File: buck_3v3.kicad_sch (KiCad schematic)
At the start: 20 parts, among them U6 TPS564257DRLR

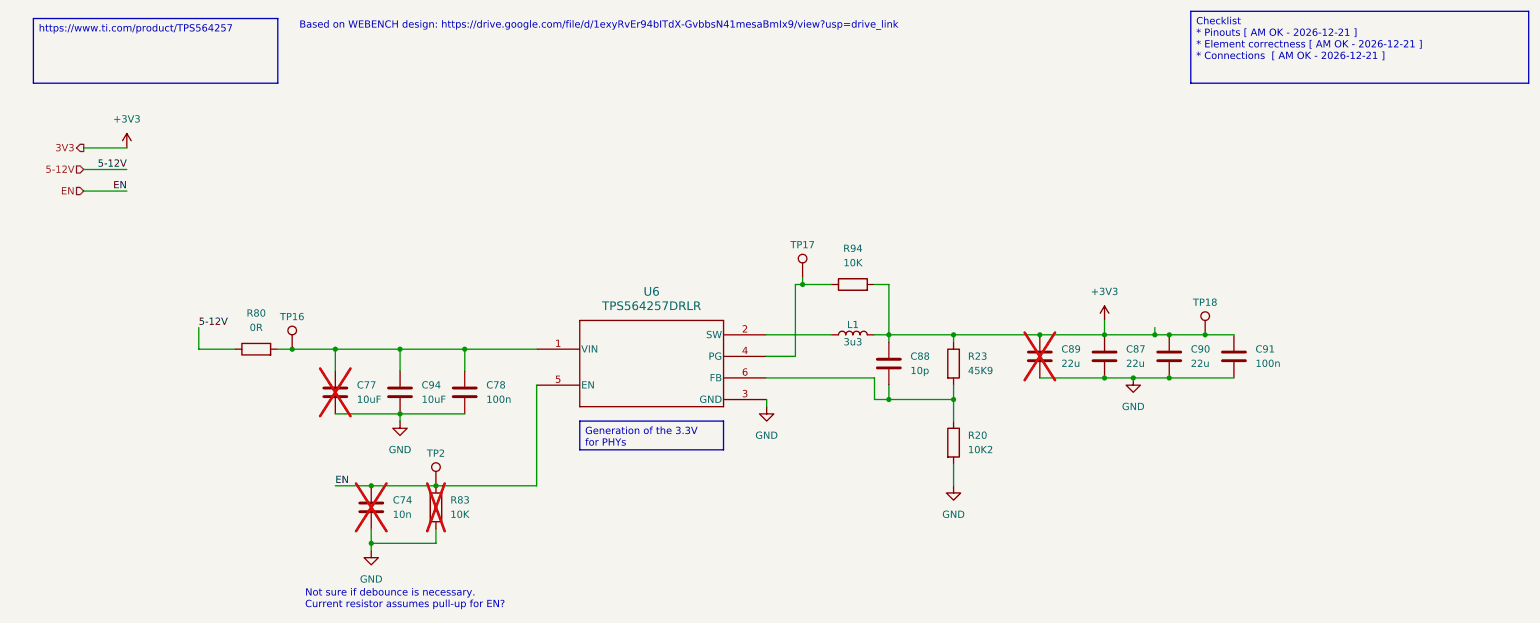
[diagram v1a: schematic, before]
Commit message: updates resistors and inductor symbol in 3V3 converter
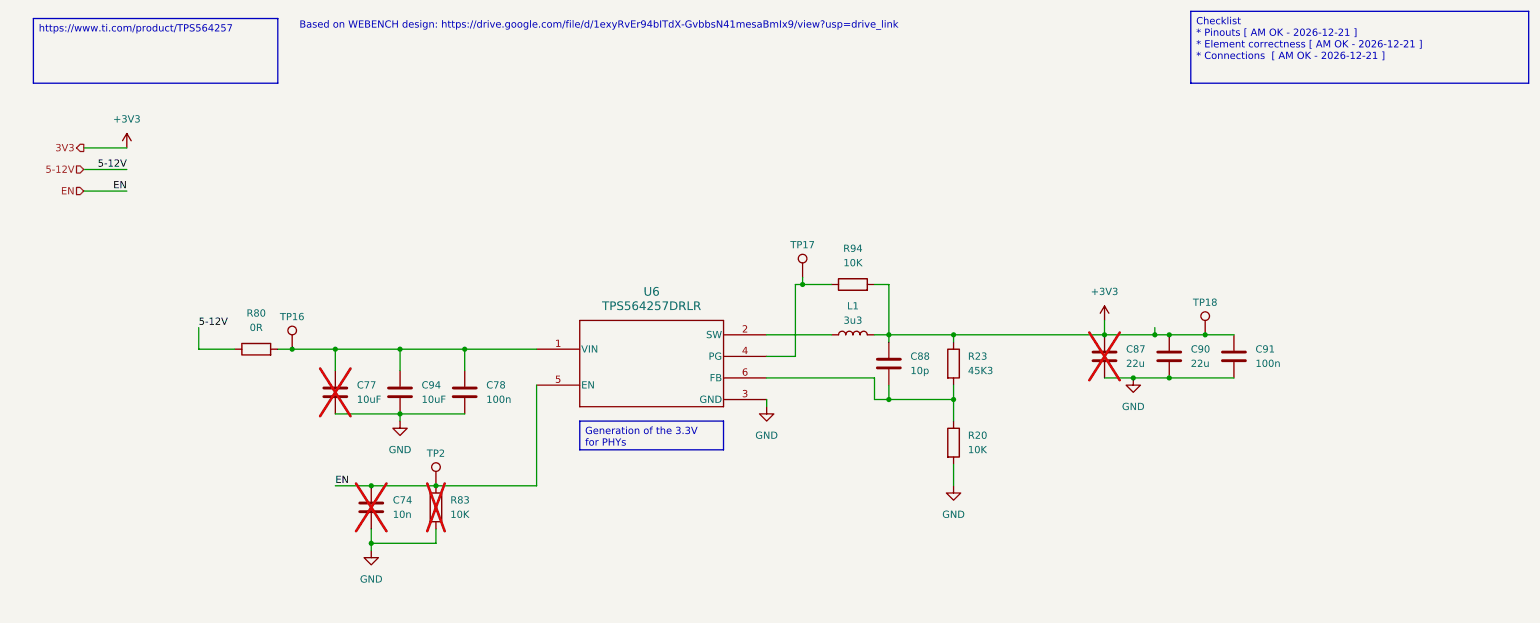
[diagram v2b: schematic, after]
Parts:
- removed C89: 22u, KL:C_0603, symbol KL_C:C_22u_10V_X5R_0603_20
- removed R20: 10K2, KL_Footprints:C_0603, symbol KL_R:R_10K2_100mW_1_0603
- removed R23: 45K9, KL_Footprints:C_0603, symbol KL_R:R_45K9_125mW_1_0603
- added R20: 10K, KL_Footprints:C_0603, symbol KL_R:R_10K_100mW_1_0603
- added R23: 45K3, KL_Footprints:C_0603, symbol KL_R:R_45K3_100mW_1_0603
- C74, C77, R83: now left out of the parts list
- C87: now not fitted; now left out of the parts list
- L1: symbol KL_L:L_3u3_8A -> KL_L:L_3u3_8A_20pct_7LX7W; I_max_in_A (none) -> 8; Max Current 8 -> (none); Package_in_mm (none) -> L7XW7; Tolerance_in_pct (none) -> 20
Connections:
- net +3V3: now also R23.1
- net GND: now also R20.2
- net at C88.2, U6.6 (FB): now also R20.1, R23.2
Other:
- note removed: "Not sure if debounce is necessary. Current resistor assumes pull-up for EN?"

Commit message: moves +3V3 converter to root. Refs: #1
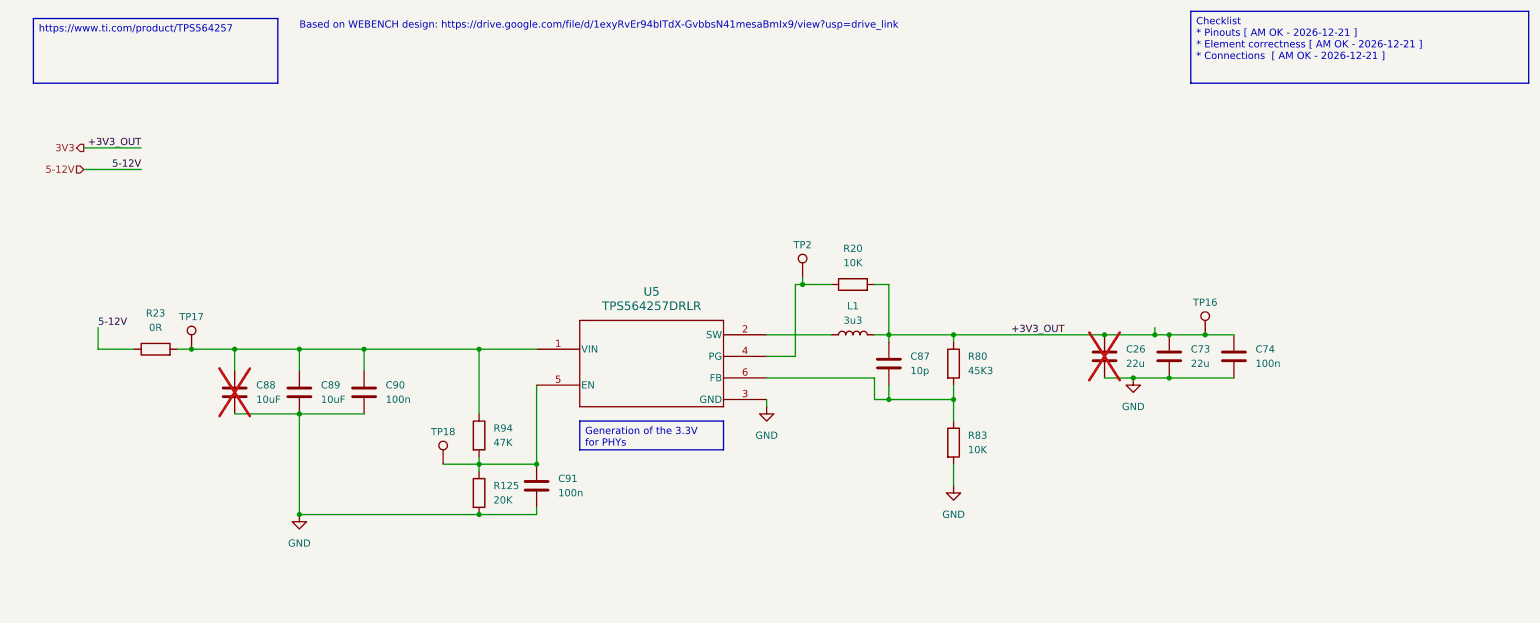
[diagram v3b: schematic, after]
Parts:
- removed C74: 10n, Capacitor_SMD:C_0201_0603Metric, symbol KL_C:C_10n_50V_X7R_0603_10
- removed R83: 10K, KL_Footprints:C_0603, symbol KL_R:R_10K_100mW_5_0603
- added C91: 100n, Capacitor_SMD:C_0201_0603Metric, symbol KL_C:C_100n_50V_X7R_0603_10
- added R125: 20K, KL_Footprints:R_0603, symbol KL_R:R_20K_100mW_1_0603
- added R94: 47K, KL_Footprints:R_0603, symbol KL_R:R_47K_100mW_1_0603
- renumbered C87 to C26, C90 to C73, C91 to C74, C88 to C87, C77 to C88, C94 to C89, C78 to C90, R94 to R20, R80 to R23, R23 to R80, R20 to R83, TP18 to TP16, TP16 to TP17, TP2 to TP18, TP17 to TP2, U6 to U5
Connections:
- net GND: now also C91.2, R125.2
- net at C88.1, C89.1, C90.1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: now also R94.1
- net +3V3 renamed 3V3
- net EN: no longer names the net of TP18.1, U5.5 (EN)
- net EN: now also C91.1, R125.1, R94.2
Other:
- moved on the sheet: C88, C89, C90, R23, TP17, TP18

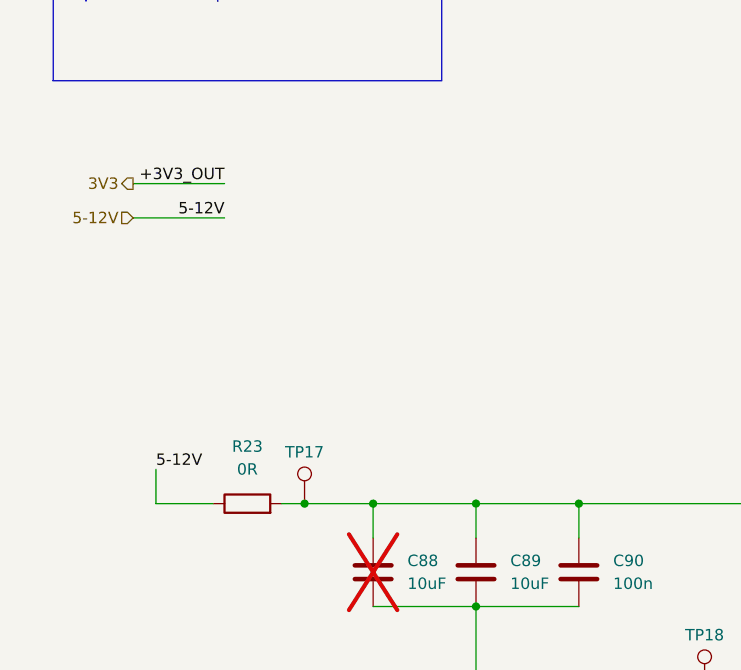
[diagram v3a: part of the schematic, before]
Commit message: fixes ERC errors in DC/DC converters
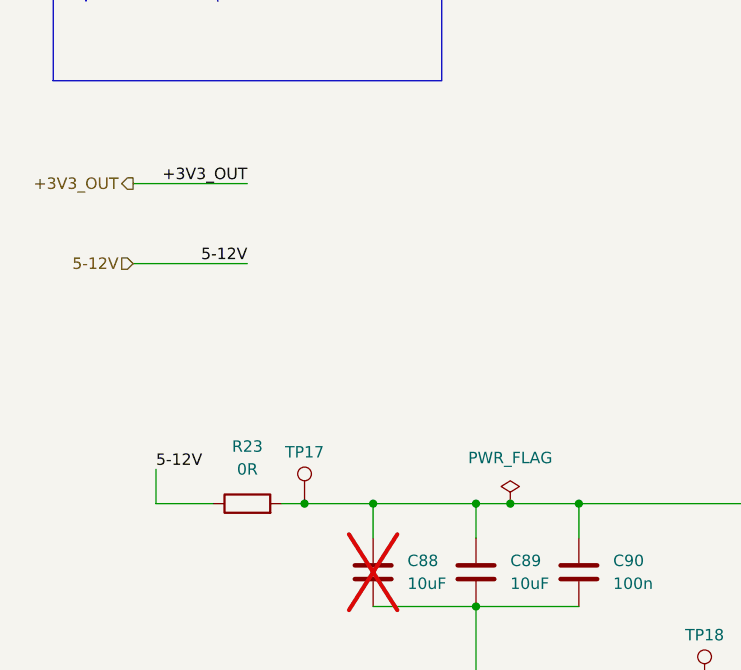
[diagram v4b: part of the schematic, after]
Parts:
- C26: footprint KL:C_0603 -> KL_Footprints:C_0603; now in the parts list
- C73: footprint KL:C_0603 -> KL_Footprints:C_0603
- C74, C87, C89, C90, C91: footprint Capacitor_SMD:C_0201_0603Metric -> KL_Footprints:C_0603
- C88: footprint Capacitor_SMD:C_0201_0603Metric -> KL_Footprints:C_0603; now in the parts list
- L1: footprint KL:L_3u3_EXLA1V0603 -> KL_Footprints:EXLA1V0603
- R20, R80, R83: footprint KL_Footprints:C_0603 -> KL_Footprints:R_0603
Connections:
- net 3V3 renamed +3V3_OUT
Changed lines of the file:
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@@
+	)
+	(junction
+		(at 68.58 74.93)
+		(diameter 0)
+		(color 0 0 0 0)
 	)
 	(junction
@@
 	(wire
 		(pts
-			(xy 76.2 74.93) (xy 64.77 74.93)
+			(xy 76.2 74.93) (xy 68.58 74.93)
 		)
 		(stroke
@@
 	(wire
 		(pts
+			(xy 26.67 39.37) (xy 39.37 39.37)
+		)
+		(stroke
+			(width 0)
+			(type default)
+		)
+	)
+	(wire
+		(pts
 			(xy 147.32 76.2) (xy 152.4 76.2)
 		)
@@
 	(wire
 		(pts
+			(xy 68.58 74.93) (xy 64.77 74.93)
+		)
+		(stroke
+			(width 0)
+			(type default)
+		)
+	)
+	(wire
+		(pts
 			(xy 168.91 83.82) (xy 180.34 83.82)
 		)
@@
 	(wire
 		(pts
-			(xy 26.67 39.37) (xy 36.83 39.37)
-		)
-		(stroke
-			(width 0)
-			(type default)
-		)
-	)
-	(wire
-		(pts
 			(xy 53.34 78.74) (xy 53.34 74.93)
 		)
@@
 	(wire
 		(pts
+			(xy 26.67 48.26) (xy 39.37 48.26)
+		)
+		(stroke
+			(width 0)
+			(type default)
+		)
+	)
+	(wire
+		(pts
 			(xy 212.09 80.01) (xy 218.44 80.01)
 		)
@@
 	(wire
 		(pts
-			(xy 64.77 74.93) (xy 53.34 74.93)
-		)
-		(stroke
-			(width 0)
-			(type default)
-		)
-	)
-	(wire
-		(pts
 			(xy 207.01 80.01) (xy 212.09 80.01)
 		)
@@
 	(wire
 		(pts
+			(xy 53.34 74.93) (xy 64.77 74.93)
+		)
+		(stroke
+			(width 0)
+			(type default)
+		)
+	)
+	(wire
+		(pts
 			(xy 218.44 72.39) (xy 215.9 72.39)
 		)
@@
 		)
 	)
-	(wire
-		(pts
-			(xy 26.67 43.18) (xy 36.83 43.18)
-		)
-		(stroke
-			(width 0)
-			(type default)
-		)
-	)
 	(label "+3V3_OUT"
-		(at 36.83 39.37 180)
+		(at 39.37 39.37 180)
 		(effects
 			(font
@@
 	)
 	(label "5-12V"
-		(at 36.83 43.18 180)
+		(at 39.37 48.26 180)
 		(effects
 			(font
@@
 	(hierarchical_label "5-12V"
 		(shape input)
-		(at 26.67 43.18 180)
+		(at 26.67 48.26 180)
 		(effects
 			(font
@@
 		)
 	)
-	(hierarchical_label "3V3"
+	(hierarchical_label "+3V3_OUT"
 		(shape output)
 		(at 26.67 39.37 180)
@@
 			)
 		)
-		(property "Footprint" "Capacitor_SMD:C_0201_0603Metric"
+		(property "Footprint" "KL_Footprints:C_0603"
 			(at 65.7352 86.36 0)
 			(effects
@@
 				(path "/d4536448-b109-4159-96e2-3dc21baf2d6e/b46af5b7-dd4e-4356-ae8f-8ea1d81113b6"
 					(reference "C89")
+					(unit 1)
+				)
+			)
+		)
+	)
+	(symbol
+		(lib_id "KL_Flags:PWR_FLAG")
+		(at 68.58 74.93 0)
+		(unit 1)
+		(exclude_from_sim no)
+		(in_bom yes)
+		(on_board yes)
+		(dnp no)
+		(fields_autoplaced yes)
+		(property "Reference" "#FLG3"
+			(at 68.58 73.025 0)
+			(effects
+				(font
+					(size 1.27 1.27)
+				)
+				(hide yes)
+			)
+		)
+		(property "Value" "PWR_FLAG"
+			(at 68.58 69.85 0)
+			(effects
+				(font
+					(size 1.27 1.27)
+				)
+			)
+		)
+		(property "Footprint" ""
+			(at 68.58 74.93 0)
+			(effects
+				(font
+					(size 1.27 1.27)
+				)
+				(hide yes)
+			)
+		)
+		(property "Datasheet" "~"
+			(at 68.58 74.93 0)
+			(effects
+				(font
+					(size 1.27 1.27)
+				)
+				(hide yes)
+			)
+		)
+		(property "Description" "Special symbol for telling ERC where power comes from"
+			(at 68.58 74.93 0)
+			(effects
+				(font
+					(size 1.27 1.27)
+				)
+				(hide yes)
+			)
+		)
+		(pin "1"
+		)
+		(instances
+			(project "shish-lan"
+				(path "/d4536448-b109-4159-96e2-3dc21baf2d6e/b46af5b7-dd4e-4356-ae8f-8ea1d81113b6"
+					(reference "#FLG3")
 					(unit 1)
 				)
@@
 			)
 		)
-		(property "Footprint" "Capacitor_SMD:C_0201_0603Metric"
+		(property "Footprint" "KL_Footprints:C_0603"
 			(at 169.8752 81.28 0)
 			(effects
@@
 		(unit 1)
 		(exclude_from_sim no)
-		(in_bom no)
+		(in_bom yes)
 		(on_board yes)
 		(dnp yes)
@@
 			)
 		)
-		(property "Footprint" "Capacitor_SMD:C_0201_0603Metric"
+		(property "Footprint" "KL_Footprints:C_0603"
 			(at 54.3052 86.36 0)
 			(effects
@@
 			)
 		)
-		(property "Footprint" "Capacitor_SMD:C_0201_0603Metric"
+		(property "Footprint" "KL_Footprints:C_0603"
 			(at 230.8352 80.01 0)
 			(effects
@@
 			)
 		)
-		(property "Footprint" "Capacitor_SMD:C_0201_0603Metric"
+		(property "Footprint" "KL_Footprints:C_0603"
 			(at 77.1652 86.36 0)
 			(effects
@@
 			)
 		)
-		(property "Footprint" "KL_Footprints:C_0603"
+		(property "Footprint" "KL_Footprints:R_0603"
 			(at 178.562 91.44 90)
 			(effects
@@
 			)
 		)
-		(property "Footprint" "KL_Footprints:C_0603"
+		(property "Footprint" "KL_Footprints:R_0603"
 			(at 162.56 65.278 90)
 			(effects
@@
 			)
 		)
-		(property "Footprint" "Capacitor_SMD:C_0201_0603Metric"
+		(property "Footprint" "KL_Footprints:C_0603"
 			(at 107.6452 102.87 0)
 			(effects
@@
 			)
 		)
-		(property "Footprint" "KL:L_3u3_EXLA1V0603"
+		(property "Footprint" "KL_Footprints:EXLA1V0603"
 			(at 158.75 64.77 0)
 			(effects
@@
 			)
 		)
-		(property "Footprint" "KL_Footprints:C_0603"
+		(property "Footprint" "KL_Footprints:R_0603"
 			(at 178.562 77.47 90)
 			(effects
@@
 			)
 		)
-		(property "Footprint" "KL:C_0603"
+		(property "Footprint" "KL_Footprints:C_0603"
 			(at 219.4052 80.01 0)
 			(effects
@@
 		(unit 1)
 		(exclude_from_sim no)
-		(in_bom no)
+		(in_bom yes)
 		(on_board yes)
 		(dnp yes)
@@
 			)
 		)
-		(property "Footprint" "KL:C_0603"
+		(property "Footprint" "KL_Footprints:C_0603"
 			(at 207.9752 80.01 0)
 			(effects

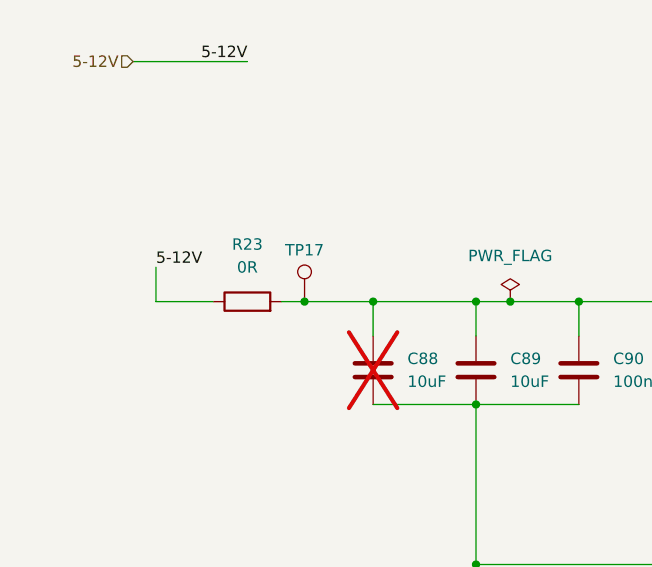
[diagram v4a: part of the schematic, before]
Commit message: removes unused busses, adds cheaper 0R resistor, clean up to fix ERC errors. Refs: #1
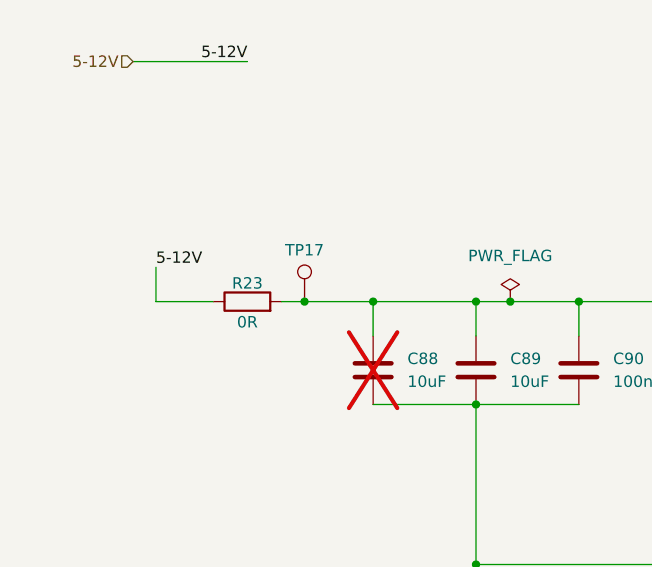
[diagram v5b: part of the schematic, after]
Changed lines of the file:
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@@
 		(on_board yes)
 		(dnp no)
-		(fields_autoplaced yes)
 		(property "Reference" "R23"
-			(at 39.37 68.58 90)
+			(at 39.37 72.898 90)
 			(effects
 				(font
@@
 		)
 		(property "Value" "0R"
-			(at 39.37 71.12 90)
+			(at 39.37 77.216 90)
 			(effects
 				(font
